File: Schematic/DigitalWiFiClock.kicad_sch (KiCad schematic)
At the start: 41 parts, among them U1 74HC595, U10 74HC595, U11 UDN2981A, U12 D148K, U13 TPIC6595, U14 D148K, U15 D148K, U16 D148K, U17 MAX7219, U18 TXS0108EPW, U2 UDN2981A, U3 TPIC6595, U4 D148K, U5 D148K, U6 D148K, U7 D148K, U8 D148K, U9 D148K

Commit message: Update testing code and hardware change
2x7seg w/ software SPI simulation
TODO: Real SPI
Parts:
- removed U18: TXS0108EPW, Package_SO:TSSOP-20_4.4x6.5mm_P0.65mm, symbol Logic_LevelTranslator:TXS0108EPW
- added MOD1: MT3608_Mod, symbol Connector_Generic:Conn_01x04
- added U19: TXS0104EPW, Package_SO:TSSOP-14_4.4x5mm_P0.65mm, symbol Logic_LevelTranslator:TXS0104EPW
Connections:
- net +3V3: now also U19.1 (V_{CCA})
- net +5V: now also MOD1.IN+ (Pin_1), U19.14 (V_{CCB}); no longer C8.2, C9.2, U11.9 (VS), U2.9 (VS)
- net GND: now also MOD1.IN- (Pin_2), U19.7 (GND); no longer C8.1, C9.1, U11.10 (GND), U2.10 (GND)
- net at A1.25 (GPIO19): now also U19.2 (A1)
- net at U17.12 (LOAD): now also U19.10 (B4)
- net at U13.12 (RCLK), U3.12 (RCLK): now also U19.11 (B3)
- net at U13.13 (SRCK), U17.13 (CLK), U3.13 (SRCK): now also U19.12 (B2)
- net at U17.1 (DIN), U3.3 (SER_IN): now also U19.13 (B1)
- net at A1.24 (GPIO18): now also U19.3 (A2)
- net at A1.26 (GPIO20): now also U19.4 (A3)
- net at A1.27 (GPIO21): now also U19.5 (A4)
- new net: C8.1, C9.1, MOD1.OUT- (Pin_4), U11.10 (GND), U2.10 (GND)
- new net: C8.2, C9.2, MOD1.OUT+ (Pin_3), U11.9 (VS), U2.9 (VS)
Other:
- moved on the sheet: U11, U2

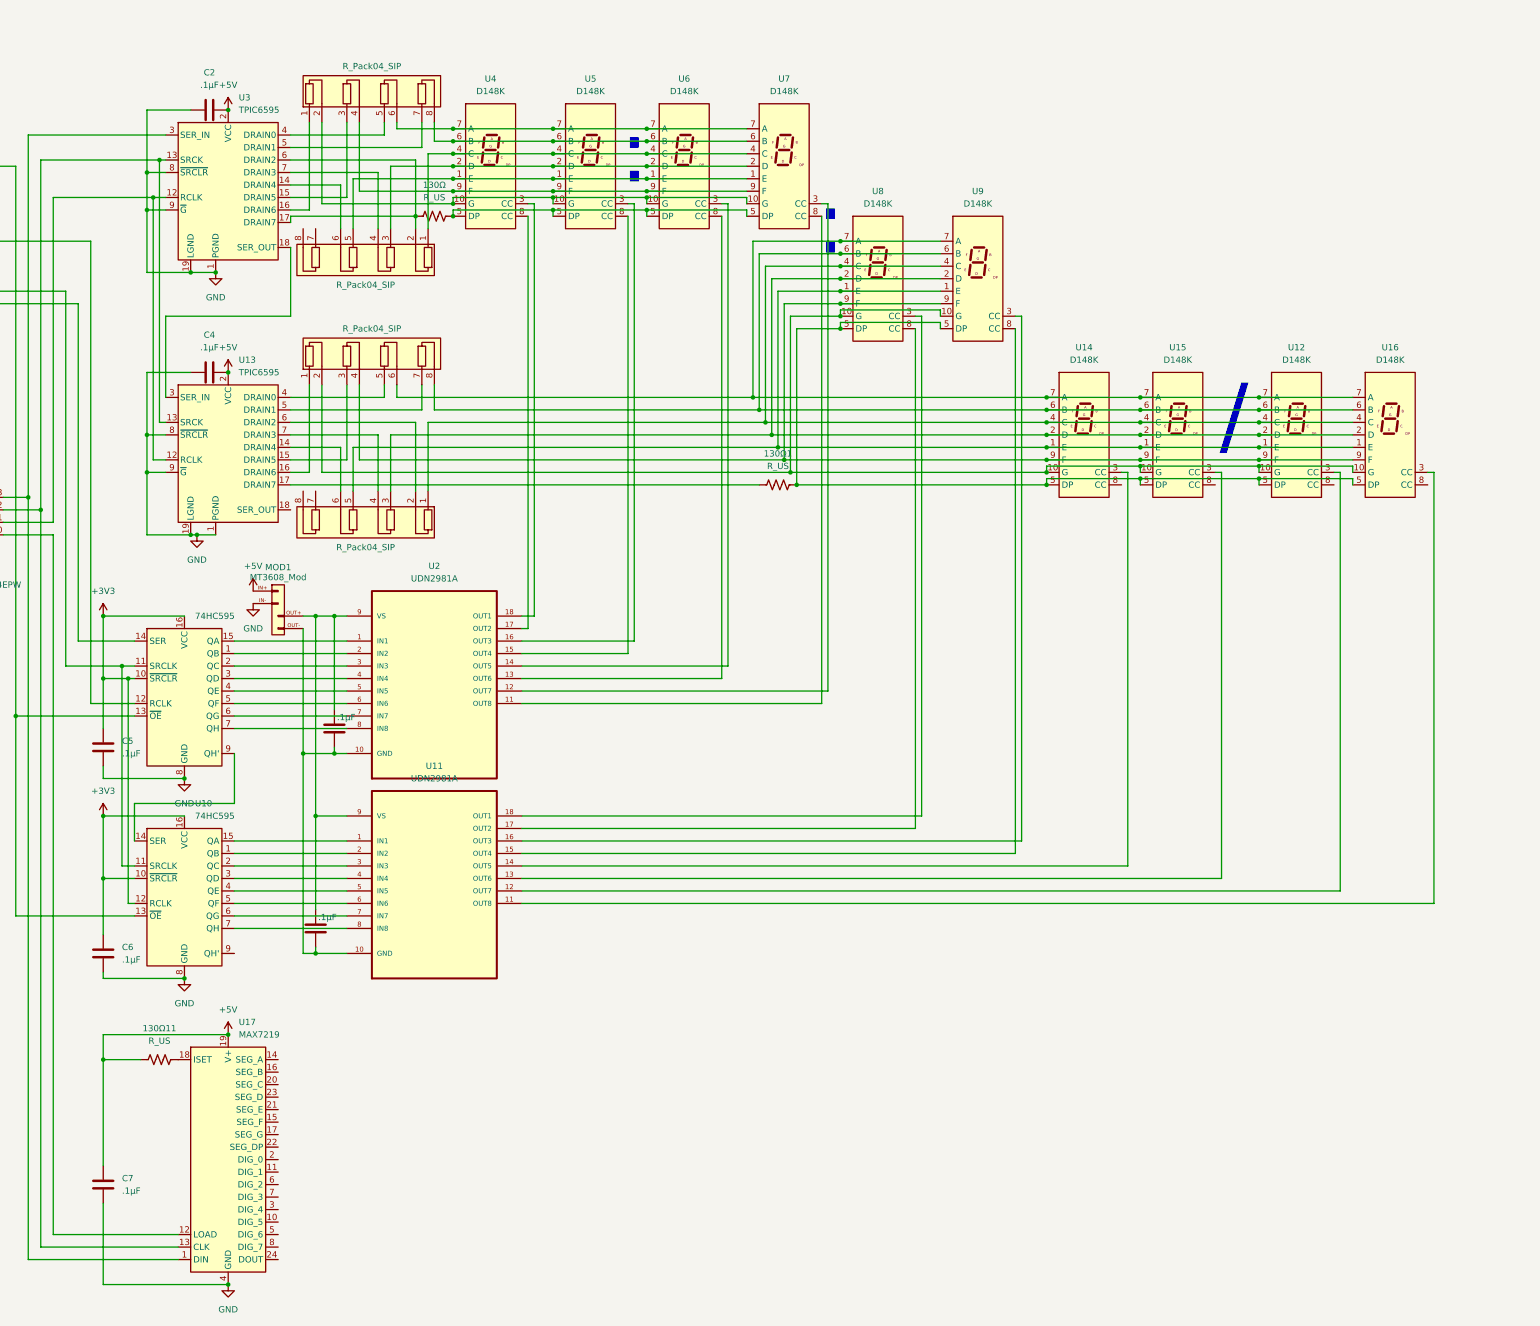
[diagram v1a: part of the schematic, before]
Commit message: Changed the whole design logic
From THT to SMD, and introduce LED-based 8 segment display and optimized 7x7 matrix display
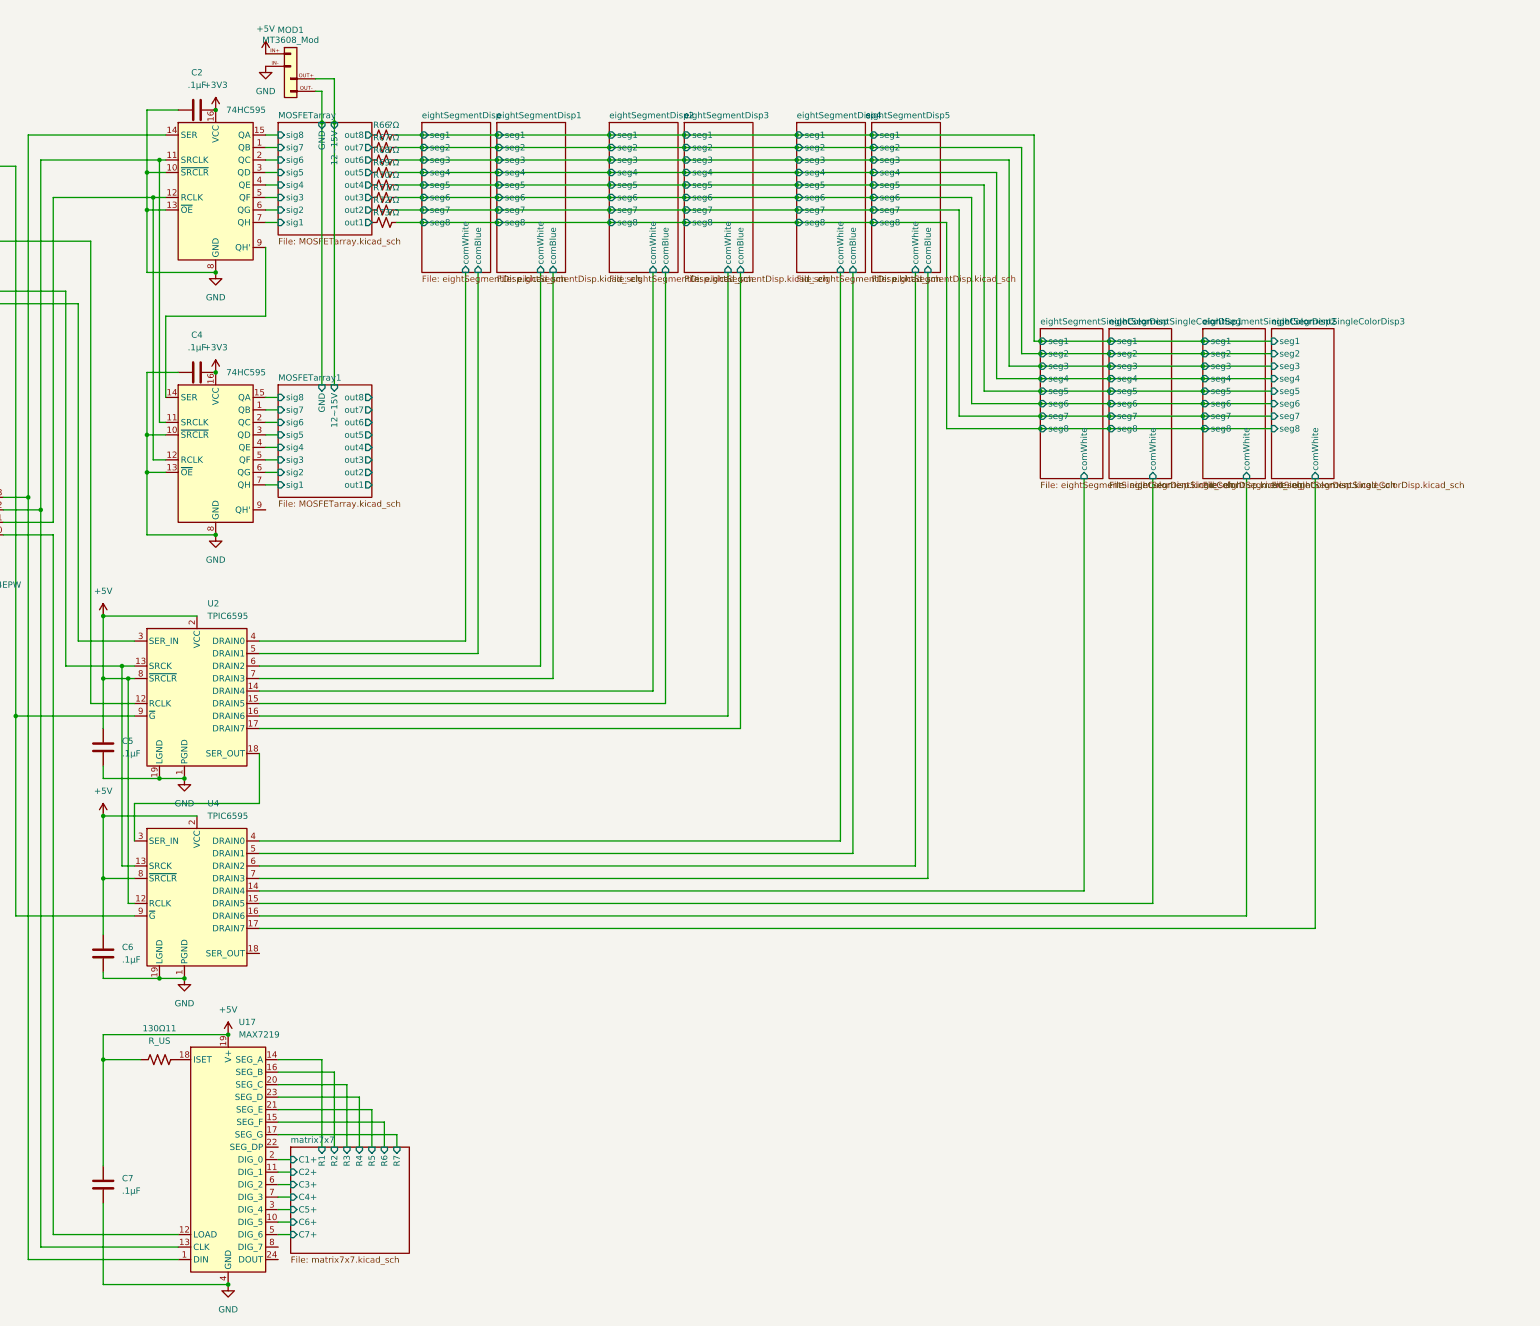
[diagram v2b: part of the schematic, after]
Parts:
- removed 130Ω, 130Ω1: R_US, symbol Device:R_US
- removed C8, C9: .1μF, symbol Device:C
- removed RN1, RN2, RN3, RN4: R_Pack04_SIP, Resistor_THT:R_Array_SIP8, symbol Device:R_Pack04_SIP
- removed U10: 74HC595, symbol 74xx:74HC595
- removed U11, U2: UDN2981A, UDN2981A:DIP254P762X533-18, symbol UDN2981A:UDN2981A
- removed U12, U14, U15, U16, U4, U5, U6, U7, U8, U9: D148K, Display_7Segment:D1X8K, symbol Display_Character:D148K
- removed U13, U3: TPIC6595, symbol Interface_Expansion:TPIC6595
- added R66, R67, R68, R69, R70, R71, R72, R73: ?Ω, symbol Device:R_Small_US
- added U2, U4: TPIC6595, symbol Interface_Expansion:TPIC6595
- added U3: 74HC595, symbol 74xx:74HC595
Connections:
- net +3V3: now also C2.2, C4.2, U3.16 (VCC); no longer C5.2, C6.2, U1.10 (~{SRCLR})
- net +5V: now also C5.2, C6.2, U2.2 (VCC), U2.8 (~{SRCLR}), U4.12 (RCLK), U4.2 (VCC), U4.8 (~{SRCLR}); no longer C2.2, C4.2
- net GND: now also U1.10 (~{SRCLR}), U1.13 (~{OE}), U2.1 (PGND), U2.10 (PGND), U2.11 (PGND), U2.19 (LGND), U2.20 (PGND), U3.10 (~{SRCLR}), U3.13 (~{OE}), U3.8 (GND), U4.1 (PGND), U4.10 (PGND), U4.11 (PGND), U4.19 (LGND), U4.20 (PGND)
- net MOSFETarray/GND: now reaches MOD1.OUT- (Pin_4)
- net MOSFETarray/12~15V: now reaches MOD1.OUT+ (Pin_3)
- net MOSFETarray/sig8: now reaches U1.15 (QA)
- net MOSFETarray/sig7: now reaches U1.1 (QB)
- net MOSFETarray/sig6: now reaches U1.2 (QC)
- net MOSFETarray/sig5: now reaches U1.3 (QD)
- net MOSFETarray/sig4: now reaches U1.4 (QE)
- net MOSFETarray/sig3: now reaches U1.5 (QF)
- net MOSFETarray/sig2: now reaches U1.6 (QG)
- net MOSFETarray/sig1: now reaches U1.7 (QH)
- net at U1.11 (SRCLK): now also U17.13 (CLK), U19.12 (B2), U3.11 (SRCLK); no longer A1.31 (GPIO26_ADC0)
- net at U1.12 (RCLK): now also U19.11 (B3), U3.12 (RCLK); no longer A1.29 (GPIO22)
- net at A1.21 (GPIO16): now also U2.9 (~{G}), U4.9 (~{G}); no longer U1.13 (~{OE})
- net at U1.14 (SER): now also U17.1 (DIN), U19.13 (B1); no longer A1.32 (GPIO27_ADC1)
- net at U1.9 (QH'): now also U3.14 (SER)
- net matrix7x7/C6+: now reaches U17.10 (DIG_5)
- net matrix7x7/C2+: now reaches U17.11 (DIG_1)
- net matrix7x7/R1: now reaches U17.14 (SEG_A)
- net matrix7x7/R6: now reaches U17.15 (SEG_F)
- net matrix7x7/R2: now reaches U17.16 (SEG_B)
- net matrix7x7/R7: now reaches U17.17 (SEG_G)
- net matrix7x7/C1+: now reaches U17.2 (DIG_0)
- net matrix7x7/R3: now reaches U17.20 (SEG_C)
- net matrix7x7/R5: now reaches U17.21 (SEG_E)
- net matrix7x7/R4: now reaches U17.23 (SEG_D)
- net matrix7x7/C5+: now reaches U17.3 (DIG_4)
- net matrix7x7/C7+: now reaches U17.5 (DIG_6)
- net matrix7x7/C3+: now reaches U17.6 (DIG_2)
- net matrix7x7/C4+: now reaches U17.7 (DIG_3)
- new net: A1.29 (GPIO22), U2.12 (RCLK)
- new net: A1.31 (GPIO26_ADC0), U2.13 (SRCK), U4.13 (SRCK)
- new net: A1.32 (GPIO27_ADC1), U2.3 (SER_IN)
- new net: U2.18 (SER_OUT), U4.3 (SER_IN)
- new net MOSFETarray/out1: R73.1
- new net MOSFETarray/out2: R72.1
- new net MOSFETarray/out3: R71.1
- new net MOSFETarray/out4: R70.1
- new net MOSFETarray/out5: R69.1
- new net MOSFETarray/out6: R68.1
- new net MOSFETarray/out7: R67.1
- new net MOSFETarray/out8: R66.1
- new net MOSFETarray1/sig1: U3.7 (QH)
- new net MOSFETarray1/sig2: U3.6 (QG)
- new net MOSFETarray1/sig3: U3.5 (QF)
- new net MOSFETarray1/sig4: U3.4 (QE)
- new net MOSFETarray1/sig5: U3.3 (QD)
- new net MOSFETarray1/sig6: U3.2 (QC)
- new net MOSFETarray1/sig7: U3.1 (QB)
- new net MOSFETarray1/sig8: U3.15 (QA)
- new net eightSegmentDisp/comBlue: U2.5 (DRAIN1)
- new net eightSegmentDisp/comWhite: U2.4 (DRAIN0)
- new net eightSegmentDisp/seg1: R66.2
- new net eightSegmentDisp/seg2: R67.2
- new net eightSegmentDisp/seg3: R68.2
- new net eightSegmentDisp/seg4: R69.2
- new net eightSegmentDisp/seg5: R70.2
- new net eightSegmentDisp/seg6: R71.2
- new net eightSegmentDisp/seg7: R72.2
- new net eightSegmentDisp/seg8: R73.2
- new net eightSegmentDisp1/comBlue: U2.7 (DRAIN3)
- new net eightSegmentDisp1/comWhite: U2.6 (DRAIN2)
- new net eightSegmentDisp2/comBlue: U2.15 (DRAIN5)
- new net eightSegmentDisp2/comWhite: U2.14 (DRAIN4)
- new net eightSegmentDisp3/comBlue: U2.17 (DRAIN7)
- new net eightSegmentDisp3/comWhite: U2.16 (DRAIN6)
- new net eightSegmentDisp4/comBlue: U4.5 (DRAIN1)
- new net eightSegmentDisp4/comWhite: U4.4 (DRAIN0)
- new net eightSegmentDisp5/comBlue: U4.7 (DRAIN3)
- new net eightSegmentDisp5/comWhite: U4.6 (DRAIN2)
- new net eightSegmentSingleColorDisp/comWhite: U4.14 (DRAIN4)
- new net eightSegmentSingleColorDisp1/comWhite: U4.15 (DRAIN5)
- new net eightSegmentSingleColorDisp2/comWhite: U4.16 (DRAIN6)
- new net eightSegmentSingleColorDisp3/comWhite: U4.17 (DRAIN7)
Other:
- added sheet MOSFETarray (MOSFETarray.kicad_sch)
- added sheet MOSFETarray1 (MOSFETarray.kicad_sch)
- added sheet eightSegmentDisp (eightSegmentDisp.kicad_sch)
- added sheet eightSegmentDisp1 (eightSegmentDisp.kicad_sch)
- added sheet eightSegmentDisp2 (eightSegmentDisp.kicad_sch)
- added sheet eightSegmentDisp3 (eightSegmentDisp.kicad_sch)
- added sheet eightSegmentDisp4 (eightSegmentDisp.kicad_sch)
- added sheet eightSegmentDisp5 (eightSegmentDisp.kicad_sch)
- added sheet eightSegmentSingleColorDisp (eightSegmentSingleColorDisp.kicad_sch)
- added sheet eightSegmentSingleColorDisp1 (eightSegmentSingleColorDisp.kicad_sch)
- added sheet eightSegmentSingleColorDisp2 (eightSegmentSingleColorDisp.kicad_sch)
- added sheet eightSegmentSingleColorDisp3 (eightSegmentSingleColorDisp.kicad_sch)
- added sheet matrix7x7 (matrix7x7.kicad_sch)
- note removed: "/"
- note removed: ":"
- moved on the sheet: C2, MOD1
